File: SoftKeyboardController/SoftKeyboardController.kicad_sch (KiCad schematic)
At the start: 40 parts, among them IC1 PCA9956BTWY, J1 Barrel_Jack, J2 Conn_01x08_Socket, J3 Motor 1, J4 Motor 2, J5 Conn_01x12_Socket, J6 Conn_01x12_Socket, J7 EXT IMU Connection, J8 Conn_01x08_Socket, Q1 Q_NMOS_GDS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

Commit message: Shrink Footprint
Relocated and re-traced board to improve overall footprint
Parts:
- removed Q1, Q10, Q11, Q12, Q13, Q14, Q15, Q16, Q2, Q3, Q4, Q5, Q6, Q7, Q8, Q9: Q_NMOS_GDS, Package_TO_SOT_THT:TO-92_Inline, symbol Transistor_FET:Q_NMOS_GDS
- added R7: 3.3kΩ, Resistor_SMD:R_0805_2012Metric, symbol Device:R_Small_US
- J1: footprint Connector_BarrelJack:BarrelJack_SwitchcraftConxall_RAPC10U_Horizontal -> Connector_BarrelJack:BarrelJack_Kycon_KLDX-0202-xC_Horizontal
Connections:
- net GND: now also R7.1
- net at U4.8 (IO0_4): now also J2.5 (Pin_5), U2.12 (IN4)
- net at J8.4 (Pin_4), U3.12 (IN4): now also U4.17 (IO1_4)
- net at J2.7 (Pin_7), U2.10 (IN6): now also U4.10 (IO0_6)
- net at J2.6 (Pin_6), U2.11 (IN5): now also U4.9 (IO0_5)
- net at J2.4 (Pin_4), U2.13 (IN3): now also U4.7 (IO0_3)
- net at J2.3 (Pin_3), U2.14 (IN2): now also U4.6 (IO0_2)
- net at J2.2 (Pin_2), U2.15 (IN1): now also U4.5 (IO0_1)
- net at J2.1 (Pin_1), U2.16 (IN0): now also U4.4 (IO0_0)
- net at J2.8 (Pin_8), U2.9 (IN7): now also U4.11 (IO0_7)
- net at J8.2 (Pin_2), U3.10 (IN6): now also U4.19 (IO1_6)
- net at U4.13 (IO1_0): now also J8.8 (Pin_8), U3.16 (IN0)
- net at U4.14 (IO1_1): now also J8.7 (Pin_7), U3.15 (IN1)
- net at U4.15 (IO1_2): now also J8.6 (Pin_6), U3.14 (IN2)
- net at U4.16 (IO1_3): now also J8.5 (Pin_5), U3.13 (IN3)
- net at U4.18 (IO1_5): now also J8.3 (Pin_3), U3.11 (IN5)
- net at U4.20 (IO1_7): now also J8.1 (Pin_1), U3.9 (IN7)
- net at IC1.1 (REXT): now also R7.2
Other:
- moved on the sheet: C1, C2, C4, C5, ESP1, IC1, J1, J2, J3, J4, J5, J6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

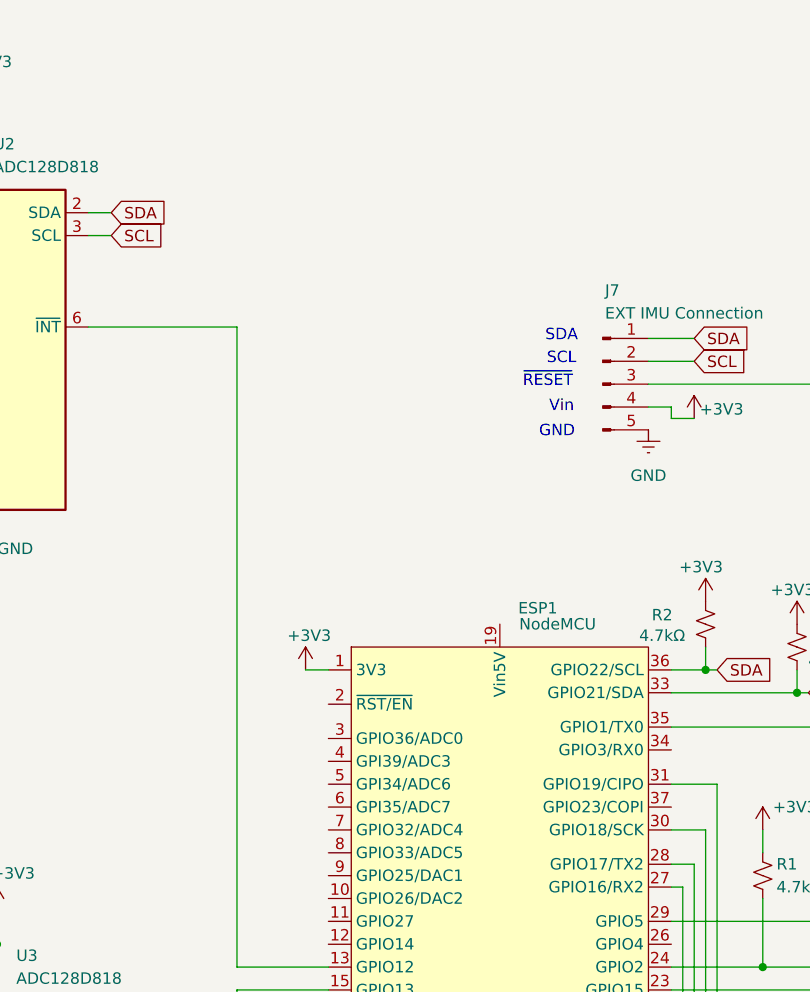
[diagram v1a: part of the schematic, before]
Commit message: Added motor encoder connections
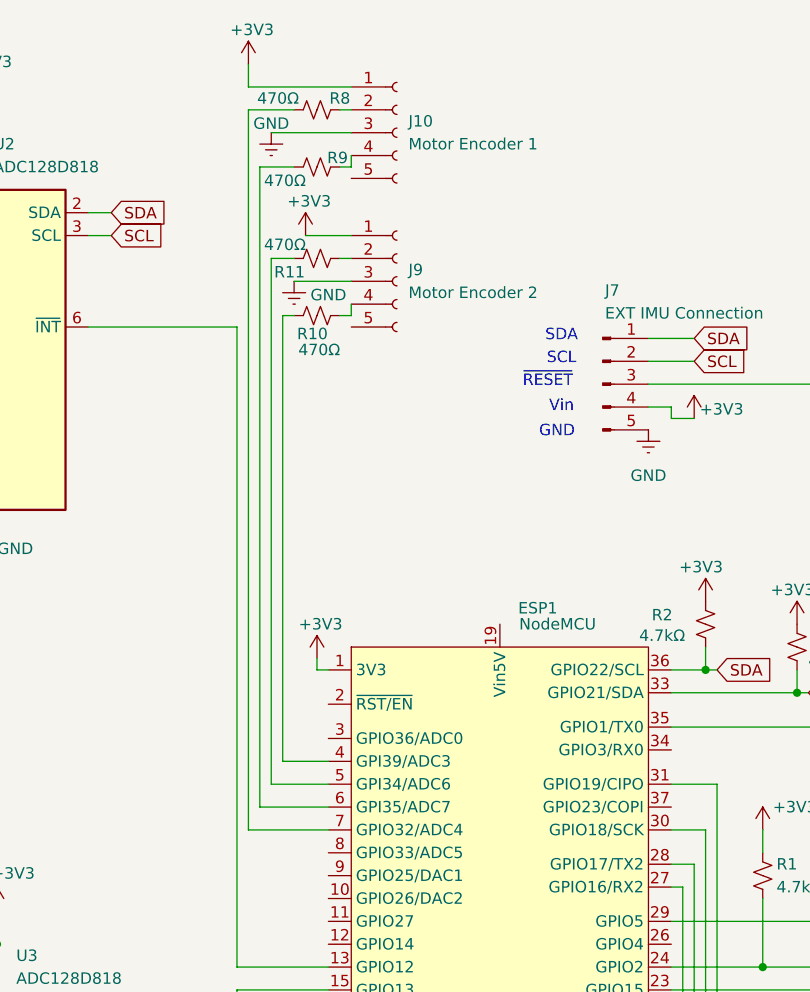
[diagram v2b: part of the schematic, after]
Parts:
- added J10: Motor Encoder 1, Connector_Molex:Molex_KK-396_A-41792-0005_1x05_P3.96mm_Horizontal, symbol Connector:Conn_01x05_Socket
- added J9: Motor Encoder 2, Connector_Molex:Molex_KK-396_A-41792-0005_1x05_P3.96mm_Horizontal, symbol Connector:Conn_01x05_Socket
- added R10, R11, R8, R9: 470Ω, Resistor_SMD:R_0805_2012Metric, symbol Device:R_Small_US
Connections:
- net +3V3: now also J10.1 (Pin_1), J9.1 (Pin_1)
- net GND: now also J10.3 (Pin_3), J9.3 (Pin_3)
- net at ESP1.4 (GPI39/ADC3): now also R10.1
- net at ESP1.5 (GPI34/ADC6): now also R11.1
- net at ESP1.6 (GPI35/ADC7): now also R9.1
- net at ESP1.7 (GPIO32/ADC4): now also R8.1
- new net: J9.2 (Pin_2), R11.2
- new net: J9.4 (Pin_4), R10.2
- new net: J10.2 (Pin_2), R8.2
- new net: J10.4 (Pin_4), R9.2

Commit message: Remapped Board again
Version of Board before ordering
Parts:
- removed J1: Barrel_Jack, Connector_BarrelJack:BarrelJack_Kycon_KLDX-0202-xC_Horizontal, symbol Connector:Barrel_Jack
- removed U1: Motor Driver DRV8847PWR, Package_SO:TSSOP-16_4.4x5mm_P0.65mm, symbol Driver_Motor:DRV8847PWR
- removed U4: PI4IOE5V9539LEX, Package_SO:TSSOP-24_4.4x7.8mm_P0.65mm, symbol ME507SoftKeyboardCustom:PI4IOE5V9539
- added C3: 10μF, Capacitor_SMD:C_0805_2012Metric, symbol Device:C_Small
- added C6: 2.2μF, Capacitor_SMD:C_0805_2012Metric, symbol Device:C_Small
- added H1, H2, H3, H4: MountingHole, MountingHole:MountingHole_2.5mm, symbol Mechanical:MountingHole
- added J1: Barrel_Jack_Switch, Connector_BarrelJack:BarrelJack_CUI_PJ-102AH_Horizontal, symbol Connector:Barrel_Jack_Switch
- added R12: 100, Resistor_SMD:R_0805_2012Metric, symbol Device:R_Small_US
- added R13: 10kΩ, Resistor_SMD:R_0805_2012Metric, symbol Device:R_Small_US
- added R14: 1kΩ, Resistor_SMD:R_0805_2012Metric, symbol Device:R_Small_US
- added TP1, TP10, TP11, TP2, TP3, TP4, TP5, TP6, TP7, TP8, TP9: TestPoint, TestPoint:TestPoint_Loop_D1.80mm_Drill1.0mm_Beaded, symbol Connector:TestPoint
- added U4: TL071, Package_TO_SOT_SMD:SOT-23-5, symbol Amplifier_Operational:TL071
- added U5: CD74HC4067SM, Package_SO:SSOP-24_5.3x8.2mm_P0.65mm, symbol 74xx:CD74HC4067SM
- added U6: DRV8848, Package_SO:TSSOP-16-1EP_4.4x5mm_P0.65mm, symbol Driver_Motor:DRV8848
- R1: value 4.7kΩ -> 10kΩ
- R3, R4: value 330mΩ -> 500mΩ
- renumbered J7 to J2, J2 to J7
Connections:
- net +3V3: now also TP10.1, U4.5 (V+), U5.24 (VCC); no longer J10.1 (Pin_1), J9.1 (Pin_1)
- net GND: now also J10.1 (Pin_1), J9.1 (Pin_1), C3.1, C6.1, J1.2, R12.1, R14.1, U4.2 (V-), U5.12 (GND), U6.13 (GND), U6.17 (GND); no longer J10.3 (Pin_3), J9.3 (Pin_3)
- net SCL: now also TP4.1, TP6.1, TP7.1
- net SDA: now also J2.3 (Pin_3), TP3.1, TP5.1, TP8.1; no longer J2.1 (Pin_1)
- net at J7.7 (Pin_7), U2.10 (IN6): now also U5.8 (I1)
- net at J7.6 (Pin_6), U2.11 (IN5): now also U5.7 (I2)
- net at J7.5 (Pin_5), U2.12 (IN4): now also U5.6 (I3)
- net at J7.4 (Pin_4), U2.13 (IN3): now also U5.5 (I4)
- net at J7.3 (Pin_3), U2.14 (IN2): now also U5.4 (I5)
- net at J7.2 (Pin_2), U2.15 (IN1): now also U5.3 (I6)
- net at J7.1 (Pin_1), U2.16 (IN0): now also U5.2 (I7)
- net at U2.6 (~{INT}): now also ESP1.4 (GPI39/ADC3); no longer ESP1.13 (GPIO12)
- net at J7.8 (Pin_8), U2.9 (IN7): now also U5.9 (I0)
- net at C1.1, C2.2: now also C3.2, J1.1, TP11.1, U6.12 (VM)
- net at J4.1 (Pin_1): now also U6.5 (BOUT2)
- net at J4.2 (Pin_2): now also U6.7 (BOUT1)
- net s0: now reaches ESP1.10 (GPIO26/DAC2)
- net s0: now also U5.10 (S0)
- net at ESP1.11 (GPIO27): now also R9.1
- net at ESP1.12 (GPIO14): now also R8.1
- net at ESP1.15 (GPIO13): now also R11.1; no longer U3.6 (~{INT})
- net 5v: now reaches ESP1.19 (Vin5V)
- net 5v: now also J10.4 (Pin_4), J9.4 (Pin_4), TP9.1
- net at ESP1.24 (GPIO2): now also U6.1 (~{SLEEP}); no longer R1.2
- net at ESP1.26 (GPIO4): now also R1.2, U6.8 (~{FAULT})
- net at ESP1.27 (GPIO16/RX2): now also U6.10 (BIN2)
- net at ESP1.28 (GPIO17/TX2): now also U6.9 (BIN1)
- net I_Op: now reaches ESP1.3 (GPIO36/ADC0)
- net I_Op: now also R13.2, TP1.1, U4.1
- net at ESP1.30 (GPIO18/SCK): now also U6.15 (AIN2)
- net at ESP1.31 (GPIO19/CIPO): now also U6.16 (AIN1)
- net at ESP1.35 (GPIO1/TX0), IC1.35 (~{RESET}), R5.2: now also J2.1 (Pin_1); no longer J2.3 (Pin_3)
- net at R10.1: now also ESP1.13 (GPIO12); no longer ESP1.4 (GPI39/ADC3)
- net at ESP1.5 (GPI34/ADC6): now also U3.6 (~{INT}); no longer R11.1
- net ~{Multi}: now reaches ESP1.6 (GPI35/ADC7)
- net ~{Multi}: now also U5.15 (~{E}); no longer R9.1
- net s3: now reaches ESP1.7 (GPIO32/ADC4)
- net s3: now also U5.13 (S3); no longer R8.1
- net s2: now reaches ESP1.8 (GPIO33/ADC5)
- net s2: now also U5.14 (S2)
- net s1: now reaches ESP1.9 (GPIO25/DAC1)
- net s1: now also U5.11 (S1)
- net at J8.8 (Pin_8), U3.16 (IN0): now also U5.16 (I15)
- net at J8.7 (Pin_7), U3.15 (IN1): now also U5.17 (I14)
- net at J8.6 (Pin_6), U3.14 (IN2): now also U5.18 (I13)
- net at J8.5 (Pin_5), U3.13 (IN3): now also U5.19 (I12)
- net at J8.4 (Pin_4), U3.12 (IN4): now also U5.20 (I11)
- net at J8.3 (Pin_3), U3.11 (IN5): now also U5.21 (I10)
- net at J8.2 (Pin_2), U3.10 (IN6): now also U5.22 (I9)
- net at J8.1 (Pin_1), U3.9 (IN7): now also U5.23 (I8)
- net at J3.1 (Pin_1): now also U6.2 (AOUT1)
- net at R3.2: now also U6.3 (AISEN)
- net at J3.2 (Pin_2): now also U6.4 (AOUT2)
- net at R4.2: now also U6.6 (BISEN)
- net at J9.2 (Pin_2): no longer R11.2
- net at R10.2: now also J9.5 (Pin_5); no longer J9.4 (Pin_4)
- net at R8.2: now also J10.3 (Pin_3); no longer J10.2 (Pin_2)
- net at R9.2: now also J10.5 (Pin_5); no longer J10.4 (Pin_4)
- new net: C6.2, U6.11 (VREF), U6.14 (VINT)
- new net: R12.2, TP2.1, U4.3 (+), U5.1 (COM)
- new net: J9.3 (Pin_3), R11.2
- new net: R13.1, R14.2, U4.4 (-)
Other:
- moved on the sheet: C1, C2, C4, C5, ESP1, IC1, J10, J2, J3, J4, J5, J6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

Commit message: changed capacitor footprint to reflect actual capacitor
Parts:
- C1: footprint Capacitor_THT:CP_Radial_D8.0mm_P3.50mm -> Capacitor_THT:CP_Radial_D10.0mm_P5.00mm
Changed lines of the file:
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@@
 			)
 		)
-		(property "Footprint" "Capacitor_THT:CP_Radial_D8.0mm_P3.50mm"
+		(property "Footprint" "Capacitor_THT:CP_Radial_D10.0mm_P5.00mm"
 			(at 271.78 124.46 0)
 			(effects
